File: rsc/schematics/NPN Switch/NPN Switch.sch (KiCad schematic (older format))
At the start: 3 parts, among them Q1 Q_NPN_CBE

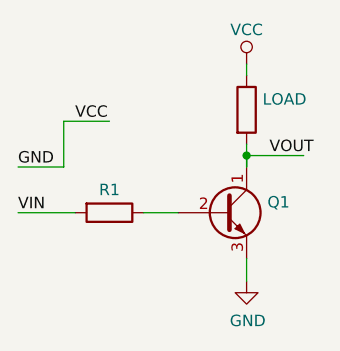
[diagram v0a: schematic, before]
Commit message: kicad v0.1 first pass generation pdf from kicad schematics still fail one sheet generation
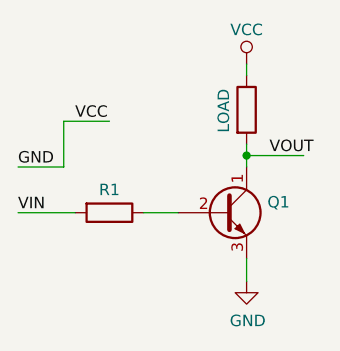
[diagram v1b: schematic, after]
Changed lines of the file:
@@
 U 1 1 5EC35F6C
 P 6000 2700
-F 0 "LOAD" H 6070 2746 50  0000 L CNN
+F 0 "LOAD" V 5900 2600 50  0000 L CNN
 F 1 "R" H 6070 2655 50  0001 L CNN
 F 2 "" V 5930 2700 50  0001 C CNN
@@
 	5550 3150 5700 3150
 Wire Wire Line
-	6000 2850 6000 2950
+	6000 2850 6000 2900
 Wire Wire Line
 	6000 2500 6000 2550
